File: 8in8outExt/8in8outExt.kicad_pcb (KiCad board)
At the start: 2 copper layers, 100.1 x 43.2 mm, 50 parts, among them P1 CONN_10X2, SW1 SPST, SW2 SPST, SW3 SPST, SW4 SPST, SW5 SPST, SW6 SPST, SW7 SPST, SW8 SPST, U1 ULN2803, U2 ULN2803

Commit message: mise ? jour serigraphie
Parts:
- moved logo_xplduino 17.4 mm to (106.9, 107.7), turned to 0 degrees
- moved R18 6.73 mm to (135.9, 97.5)
- moved D17 4.62 mm to (135.9, 93.2), turned to 0 degrees
- moved D18 1.65 mm to (135.9, 97.5), turned to 0 degrees
- moved R17 0.13 mm to (135.9, 93.2)
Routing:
- net LED: track 20.4 -> 15.7 mm
- net N-0000028: track 7.99 -> 4.16 mm
- net N-0000030: track 5.03 -> 4.04 mm
- net +5V: track 199.8 -> 199.1 mm
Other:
- board outline removed
- board text added: "NORM"
- board text added: "NORMAL"
- board text added: "home automation"

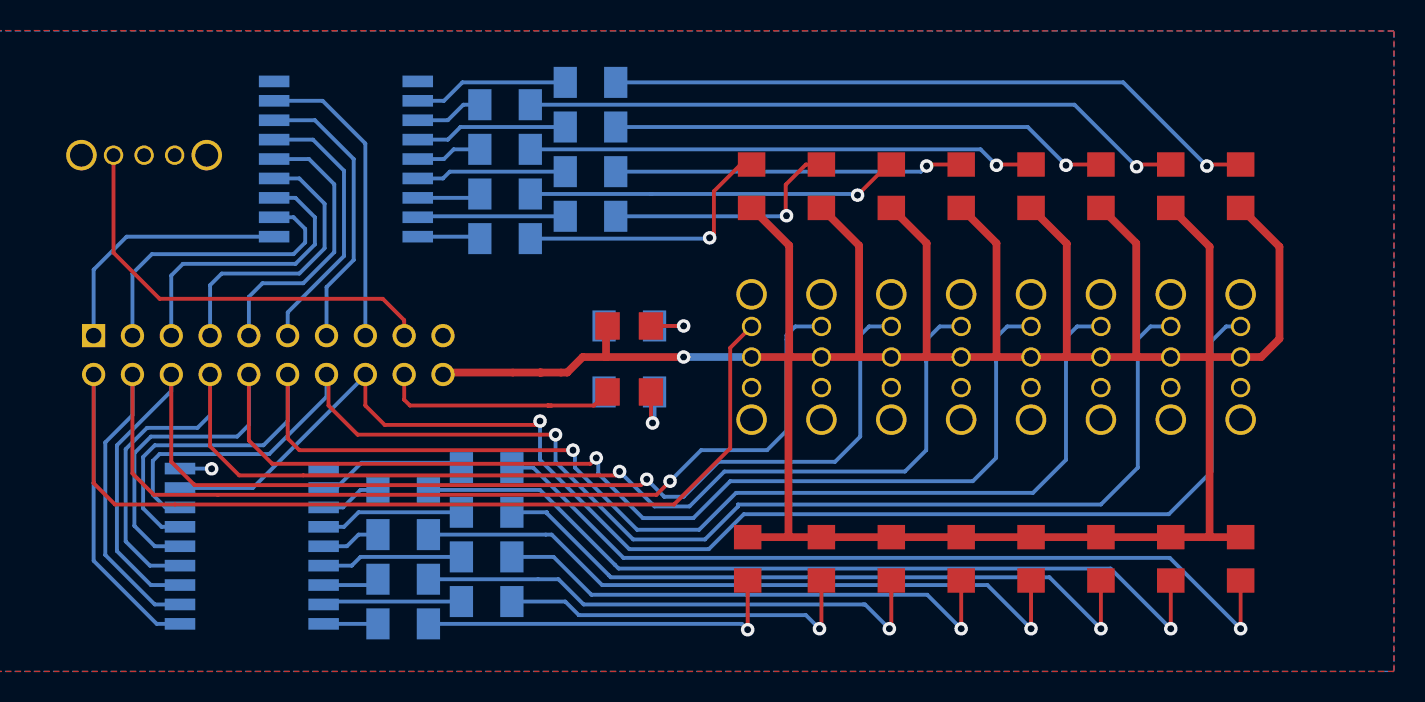
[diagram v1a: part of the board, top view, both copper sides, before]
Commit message: remplacement leds cms par led 3 mm reamenagement position leds et switchs reprise serigraphie
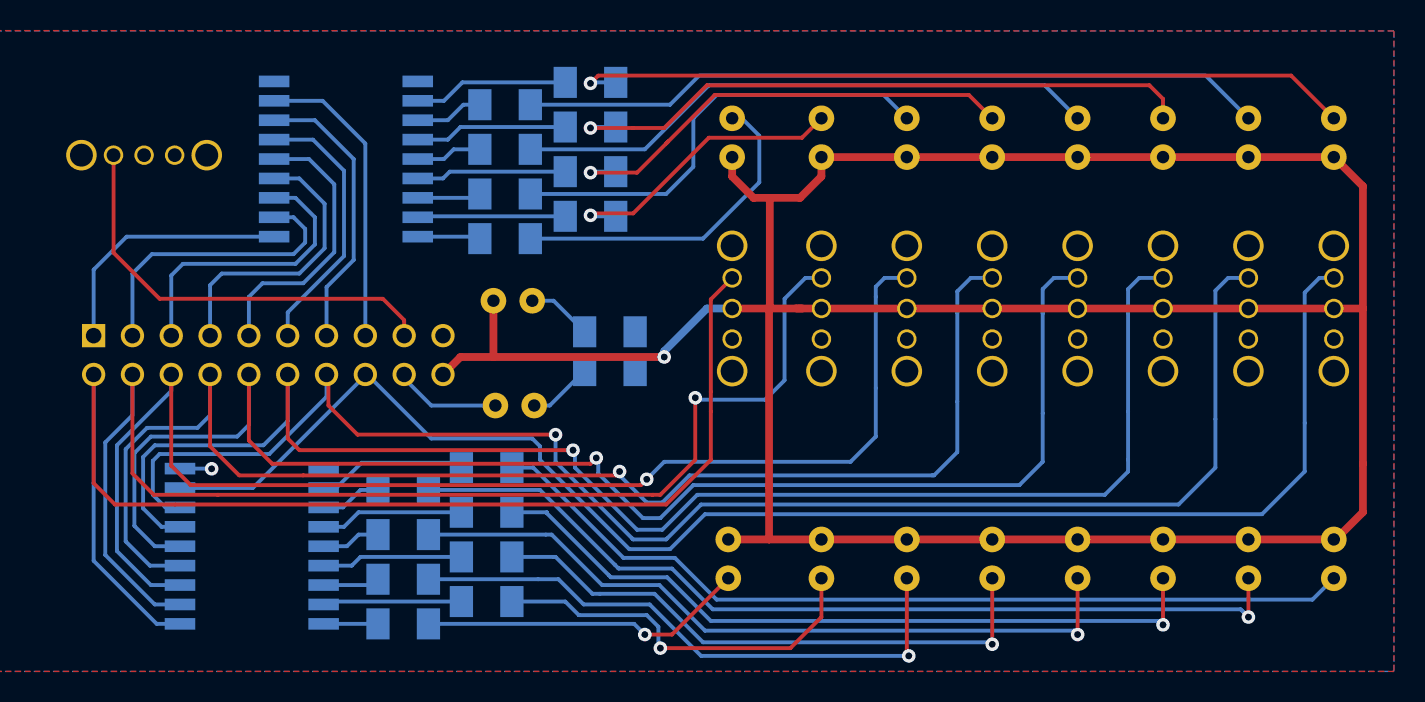
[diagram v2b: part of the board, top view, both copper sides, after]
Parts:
- removed the logo_xplduino at (93.3, 95.8)
- D1, D10, D11, D12, D13, D14, D15, D16, D17, D18, D2, D3, D4, D5, D6, D7, D8, D9: footprint LED-1206 -> LED-3MM
- moved logo_xplduino 9.11 mm to (97.9, 106.4)
- moved D17 7.80 mm to (128.3, 91.6)
- moved D18 7.55 mm to (128.4, 98.4)
- moved D8 6.87 mm to (182.0, 80.9)
- moved SW8 6.87 mm to (182.0, 92.1)
- moved D16 6.10 mm to (182.0, 108.5)
- moved D7 5.99 mm to (176.4, 80.9)
- moved SW7 5.99 mm to (176.4, 92.1)
- moved D6 5.16 mm to (170.8, 80.9)
- moved SW6 5.16 mm to (170.8, 92.1)
- moved D15 5.08 mm to (176.4, 108.5)
- moved D5 4.40 mm to (165.2, 80.9)
- moved SW5 4.40 mm to (165.2, 92.1)
- moved D14 4.06 mm to (170.8, 108.5)
- moved D4 3.77 mm to (159.6, 80.9)
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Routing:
- net N-0000048: track 32.8 -> 41.9 mm
- net LED: track 15.7 -> 6.96 mm
- net N-0000049: track 43.2 -> 51.7 mm
- net OUT6: track 91.6 -> 99.7 mm
- net N-0000044: track 22.8 -> 30.9 mm
- net OUT5: track 90.4 -> 98.1 mm
- net OUT7: track 91.2 -> 98.1 mm, vias 1 -> 0
- net OUT4: track 88.1 -> 94.8 mm
- net N-0000050: track 43.7 -> 48.9 mm, vias 1 -> 0
- net N-0000052: track 24.5 -> 29.8 mm, vias 1 -> 0
- net N-0000051: track 33.2 -> 38.4 mm, vias 1 -> 0
- net OUT3: track 84.2 -> 89.4 mm
- net N-0000011: track 44.9 -> 49.1 mm
- net N-000003: track 55.5 -> 59.6 mm
- net N-000005: track 45.1 -> 49.2 mm
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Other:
- board text removed: "NORM"

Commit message: Final pour prod
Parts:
- added G***: LOGO, OSHWLOGO0.3IN, F.Cu at (91.2, 103.9)
- moved logo_xplduino 9.70 mm to (107.3, 108.8)
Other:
- board outline added: 100.1 x 42 mm
- board text added: "8in8out Extension Board v0.0"
- board text added: "MANUAL /RESET"
- board text added: "MODE"
- board text removed: "RESET"

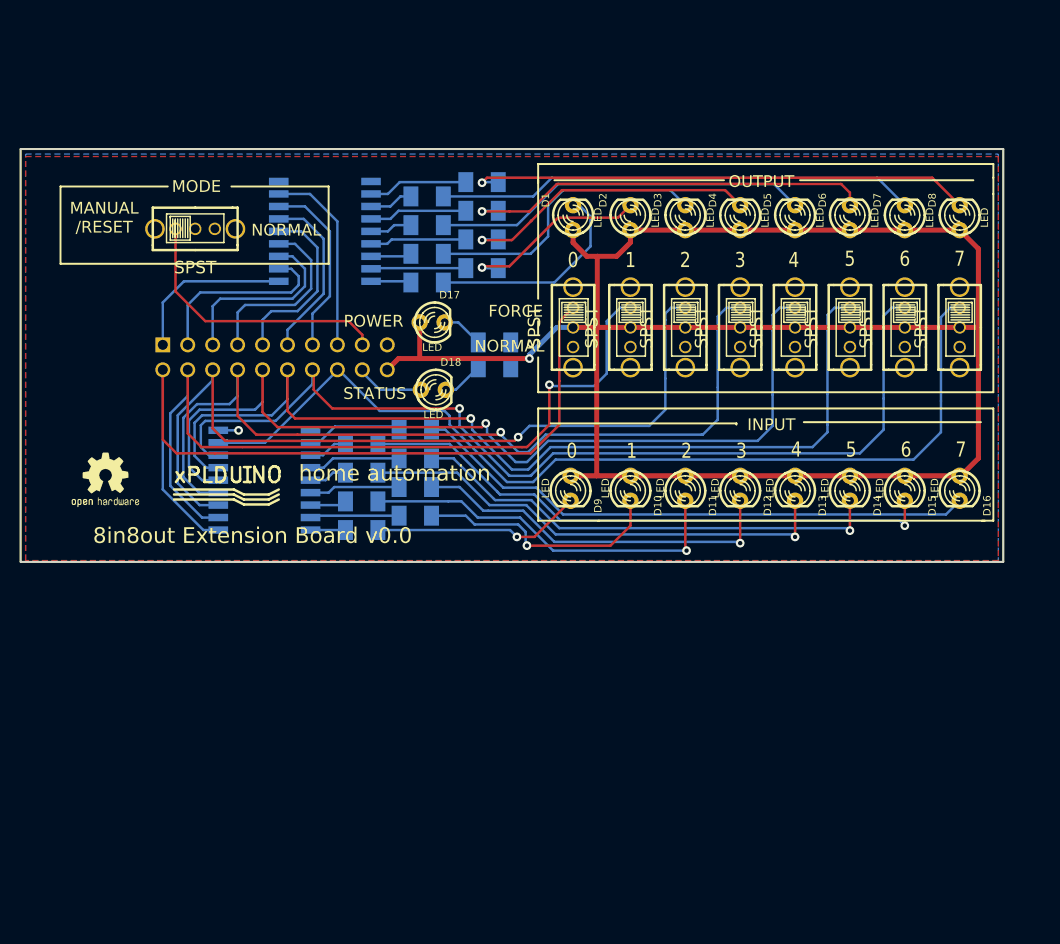
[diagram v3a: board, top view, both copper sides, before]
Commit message: ajout resistance forcage sortie routage incomplet
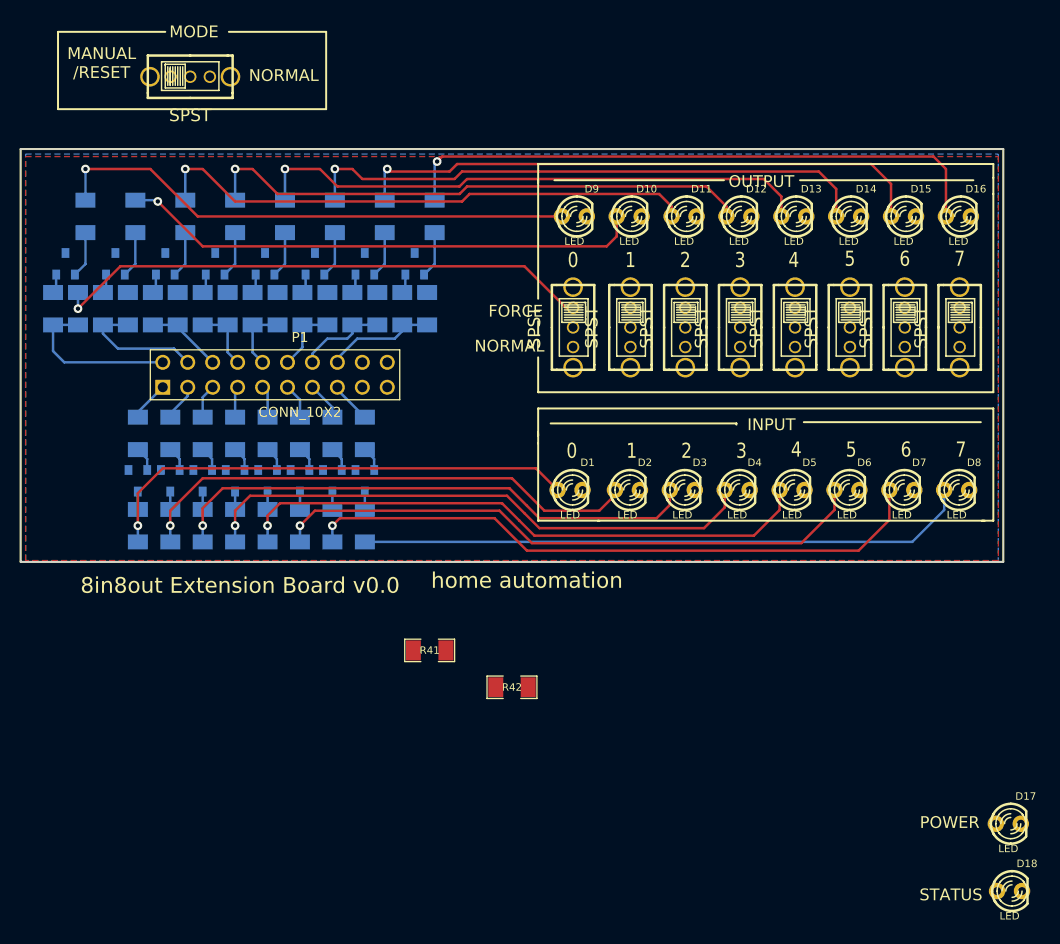
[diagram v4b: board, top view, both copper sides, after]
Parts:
- removed G***: LOGO, OSHWLOGO0.3IN
- removed U1, U2: ULN2803, SOIC18
- removed logo_xplduino: VAL**, logo_xplduino
- added Q1: PNP, SOT23, B.Cu at (98.3, 107.7)
- added Q10: NPN, SOT23, B.Cu at (96.0, 85.6)
- added Q11: NPN, SOT23, B.Cu at (101.1, 85.6)
- added Q12: NPN, SOT23, B.Cu at (106.2, 85.6)
- added Q13: NPN, SOT23, B.Cu at (111.3, 85.6)
- added Q14: NPN, SOT23, B.Cu at (116.3, 85.6)
- added Q15: NPN, SOT23, B.Cu at (121.4, 85.6)
- added Q16: NPN, SOT23, B.Cu at (126.5, 85.6)
- added Q2: PNP, SOT23, B.Cu at (101.6, 107.7)
- added Q3: PNP, SOT23, B.Cu at (104.9, 107.7)
- added Q4: PNP, SOT23, B.Cu at (108.2, 107.7)
- added Q5: PNP, SOT23, B.Cu at (111.5, 107.7)
- added Q6: PNP, SOT23, B.Cu at (114.8, 107.7)
- added Q7: PNP, SOT23, B.Cu at (118.1, 107.7)
- added Q8: PNP, SOT23, B.Cu at (121.4, 107.7)
- added Q9: NPN, SOT23, B.Cu at (90.9, 85.6)
- added R19: R, SM1206, B.Cu at (104.9, 112.3)
- added R20: R, SM1206, B.Cu at (108.2, 112.3)
- added R21: R, SM1206, B.Cu at (111.5, 112.3)
- added R22: R, SM1206, B.Cu at (114.8, 112.3)
- added R23: R, SM1206, B.Cu at (118.1, 112.3)
- added R24: R, SM1206, B.Cu at (121.4, 112.3)
- added R25: R, SM1206, B.Cu at (89.7, 90.2)
- added R26: R, SM1206, B.Cu at (94.7, 90.2)
- added R27: R, SM1206, B.Cu at (99.8, 90.2)
- added R28: R, SM1206, B.Cu at (104.9, 90.2)
- added R29: R, SM1206, B.Cu at (110.0, 90.2)
- added R30: R, SM1206, B.Cu at (115.1, 90.2)
- added R31: R, SM1206, B.Cu at (120.1, 90.2)
- added R32: R, SM1206, B.Cu at (125.2, 90.2)
- added R33: R, SM1206, B.Cu at (93.0, 80.8)
- added R34: R, SM1206, B.Cu at (98.0, 80.8)
- added R35: R, SM1206, B.Cu at (103.1, 80.8)
- added R36: R, SM1206, B.Cu at (108.2, 80.8)
- added R37: R, SM1206, B.Cu at (113.3, 80.8)
- added R38: R, SM1206, B.Cu at (118.4, 80.8)
- added R39: R, SM1206, B.Cu at (123.4, 80.8)
- added R40: R, SM1206, B.Cu at (128.5, 80.8)
- added R41: R, SM1206, F.Cu at (128.0, 125.0)
- added R42: R, SM1206, F.Cu at (136.4, 128.7)
- P1: moved to F.Cu
- moved D18 77.8 mm to (187.1, 149.5)
- moved D17 77.8 mm to (186.9, 142.6)
- moved R17 40.8 mm to (98.3, 112.3), turned to 90 degrees
- moved R18 36.7 mm to (101.6, 112.3), turned to 90 degrees
- moved R2 36.3 mm to (97.3, 90.2), turned to 270 degrees
- moved R1 35.7 mm to (92.2, 90.2), turned to 270 degrees
- moved D1 27.7 mm to (142.3, 108.6), turned to 0 degrees
- moved D2 27.7 mm to (148.2, 108.6), turned to 0 degrees
- moved D3 27.7 mm to (153.7, 108.6), turned to 0 degrees
- moved D4 27.7 mm to (159.3, 108.6), turned to 0 degrees
- moved D5 27.7 mm to (164.9, 108.6), turned to 0 degrees
- moved D6 27.7 mm to (170.5, 108.6), turned to 0 degrees
- moved D7 27.7 mm to (176.1, 108.6), turned to 0 degrees
- moved D8 27.7 mm to (181.7, 108.6), turned to 0 degrees
- moved D9 27.7 mm to (142.7, 80.8), turned to 0 degrees
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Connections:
- D1 pad 1: +5V -> N-0000055
- D1 pad 2: N-0000054 -> GND
- D10 pad 1: +5V -> N-0000011
- D10 pad 2: N-0000017 -> GND
- D11 pad 1: +5V -> N-0000047
- D11 pad 2: N-000007 -> GND
- D12 pad 1: +5V -> N-0000042
- D12 pad 2: N-0000012 -> GND
- D13 pad 1: +5V -> N-0000050
- D13 pad 2: N-000005 -> GND
- D14 pad 1: +5V -> N-0000034
- D14 pad 2: N-0000011 -> N-0000033
- D15 pad 1: +5V -> N-0000029
- D15 pad 2: N-000003 -> GND
- D16 pad 1: +5V -> N-0000037
- D16 pad 2: N-000001 -> GND
- D17 pad 2: N-0000030 -> N-0000060
- D18 pad 2: N-0000028 -> N-0000059
- D2 pad 1: +5V -> N-0000064
- D2 pad 2: N-0000047 -> GND
- D3 pad 1: +5V -> N-0000074
- D3 pad 2: N-0000052 -> GND
- D4 pad 1: +5V -> N-0000021
- D4 pad 2: N-0000044 -> GND
- D5 pad 1: +5V -> N-0000017
- D5 pad 2: N-0000051 -> GND
- D6 pad 1: +5V -> N-0000026
- D6 pad 2: N-0000048 -> GND
- D7 pad 1: +5V -> N-0000022
- D7 pad 2: N-0000050 -> GND
- D8 pad 1: +5V -> N-000006
- D8 pad 2: N-0000049 -> GND
- D9 pad 1: +5V -> N-0000014
- D9 pad 2: N-000009 -> GND
- R1 pad 1: N-0000053 -> N-0000077
- R1 pad 2: N-0000054 -> OUT0
- R10 pad 1: N-0000016 -> CMD1
- R10 pad 2: N-0000017 -> N-0000075
- R11 pad 1: N-000008 -> CMD2
- R11 pad 2: N-000007 -> N-0000071
- R12 pad 1: N-0000015 -> CMD3
- R12 pad 2: N-0000012 -> N-0000019
- R13 pad 1: N-000006 -> CMD4
- R13 pad 2: N-000005 -> N-0000015
- R14 pad 1: N-0000014 -> CMD5
- R14 pad 2: N-0000011 -> N-0000023
- R15 pad 1: N-000004 -> CMD6
- R15 pad 2: N-000003 -> N-000007
- R16 pad 1: N-000002 -> CMD7
- R17 pad 1: GND -> N-0000055
- R17 pad 2: N-0000030 -> N-0000054
- R18 pad 1: GND -> N-0000064
- R18 pad 2: N-0000028 -> N-0000063
- R2 pad 1: N-0000046 -> N-0000076
- R2 pad 2: N-0000047 -> OUT1
- R3 pad 1: N-0000045 -> N-0000073
- R3 pad 2: N-0000052 -> OUT2
- R4 pad 1: N-0000043 -> N-0000069
- R4 pad 2: N-0000044 -> OUT3
- R5 pad 1: N-0000039 -> N-0000068
- R5 pad 2: N-0000051 -> OUT4
- R6 pad 1: N-0000040 -> N-0000067
- R6 pad 2: N-0000048 -> OUT5
- R7 pad 1: N-0000041 -> N-0000066
- R7 pad 2: N-0000050 -> OUT6
- R8 pad 1: N-0000042 -> N-0000065
- R8 pad 2: N-0000049 -> OUT7
- R9 pad 1: N-0000010 -> CMD0
- R9 pad 2: N-000009 -> N-0000062
- SW1 pad 1: OUT0 -> N-0000077
- SW2 pad 1: OUT1 -> N-0000076
- SW3 pad 1: OUT2 -> N-0000073
- SW4 pad 1: OUT3 -> N-0000069
- SW5 pad 1: OUT4 -> N-0000068
- SW6 pad 1: OUT5 -> N-0000067
- SW7 pad 1: OUT6 -> N-0000066
- SW8 pad 1: OUT7 -> N-0000065
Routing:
- net +5V: track 197.5 -> 0.00 mm, vias 1 -> 0
- net OUT5: track 98.1 -> 6.98 mm, vias 1 -> 0
- net OUT6: track 99.7 -> 9.22 mm, vias 1 -> 0
- net OUT4: track 94.8 -> 6.77 mm, vias 1 -> 0
- net OUT7: track 98.1 -> 11.3 mm
- net OUT3: track 89.4 -> 6.77 mm, vias 1 -> 0
- net OUT2: track 84.1 -> 7.82 mm, vias 1 -> 0
- net OUT1: track 82.8 -> 13.3 mm, vias 1 -> 0
- net OUT0: track 81.3 -> 16.9 mm
- net N-0000022: track 0.00 -> 64.4 mm, vias 0 -> 1
- net N-0000026: track 0.00 -> 61.5 mm, vias 0 -> 1
- net N-0000037: track 0.00 -> 61.4 mm, vias 0 -> 1
- net N-0000029: track 0.00 -> 59.2 mm, vias 0 -> 1
- net N-000006: track 3.87 -> 62.4 mm
- net N-0000034: track 0.00 -> 58.5 mm, vias 0 -> 1
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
